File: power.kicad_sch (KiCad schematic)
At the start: 12 parts, among them SW3 SW_SPDT, U2 TP4054, U4 XC6206PxxxMR

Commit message: stm32g0
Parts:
- C6: value 0.1uF -> 100nF
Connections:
- net +5V: now also C6.2; no longer C6.1
- net GND: now also C6.1; no longer C6.2
- net at D5.1 (K), F1.2, U2.3 (V_{BAT}): now also SW3.3 (C); no longer SW3.1 (A)
- no-connect marks 2 -> 1
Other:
- moved on the sheet: BT1, C6

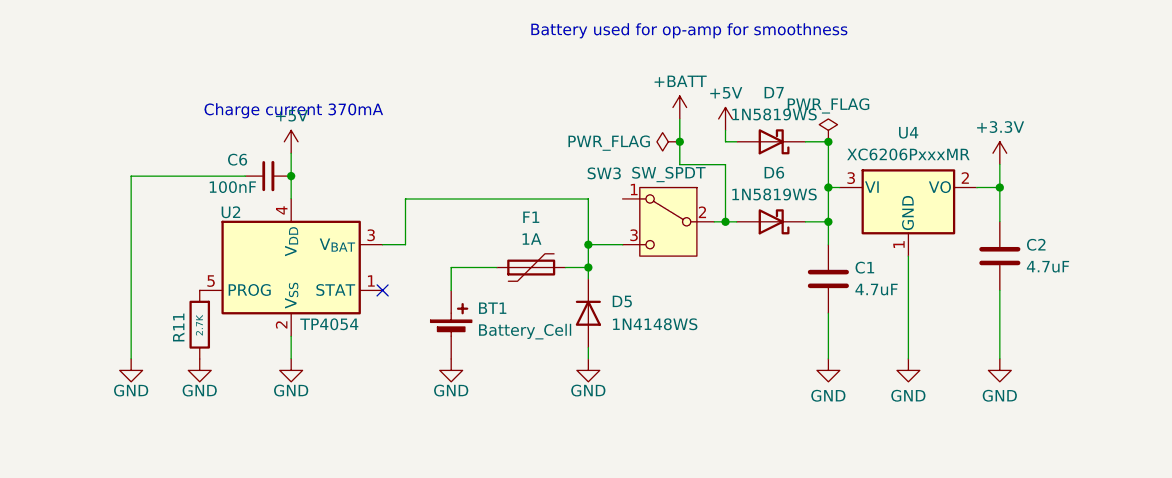
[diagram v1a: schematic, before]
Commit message: Silkscreen fixes
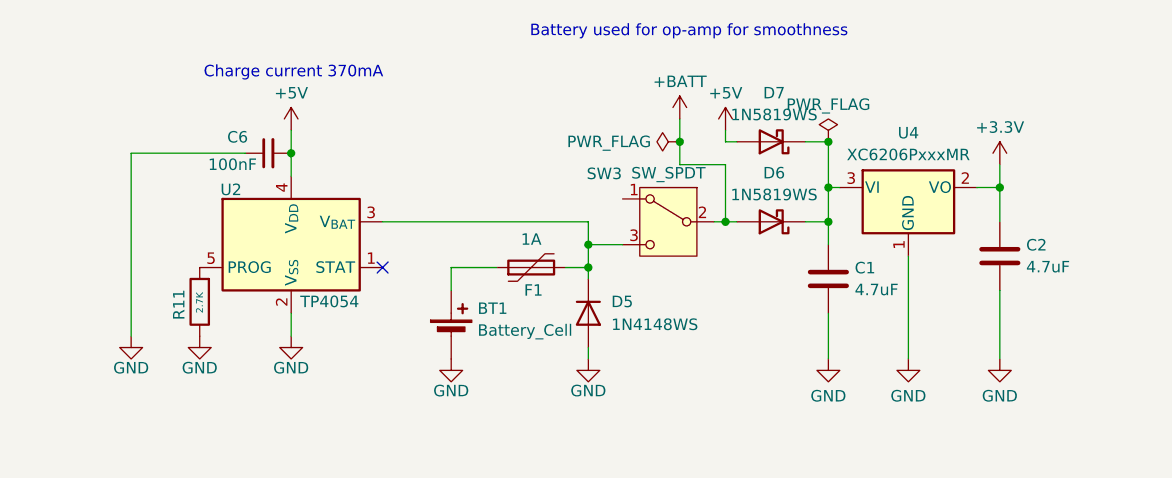
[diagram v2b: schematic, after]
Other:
- moved on the sheet: C6, R11, U2

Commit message: Added charge indicator LED, upped charge pump capacitor bank voltage rating for more headroom
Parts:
- added D1: LED, LED_SMD:LED_0805_2012Metric, symbol Device:LED
- added R1: 1K, Resistor_SMD:R_0603_1608Metric, symbol Device:R
- C1, C2: footprint Capacitor_SMD:C_0603_1608Metric_Pad1.08x0.95mm_HandSolder -> Capacitor_SMD:C_0805_2012Metric; LCSC C19666 -> C1779
- C6: value 100nF -> 1uF; LCSC C14663 -> C15849
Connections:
- net +5V: now also R1.2
- net at U2.1 (STAT): now also D1.1 (K)
- new net: D1.2 (A), R1.1
- no-connect marks 1 -> 0
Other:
- moved on the sheet: C2, R11, U2

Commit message: Fixed switch mounting holes not being grounded
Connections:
- net GND: now also SW3.4 (GND)
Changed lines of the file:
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@@
+	(wire
+		(pts
+			(xy 110.49 54.61) (xy 110.49 45.72)
+		)
+		(stroke
+			(width 0)
+			(type default)
+		)
+	)
 	(wire
 		(pts
@@
 		(in_pos_files yes)
 		(dnp no)
-		(fields_autoplaced yes)
 		(property "Reference" "D5"
-			(at 104.14 48.26 90)
+			(at 104.394 48.006 0)
 			(show_name no)
 			(do_not_autoplace no)
@@
 		)
 		(property "Value" "1N4148WS"
-			(at 104.14 50.8 90)
+			(at 106.426 48.006 0)
 			(show_name no)
 			(do_not_autoplace no)
@@
 		(pin "3"
 		)
+		(pin "4"
+		)
 		(instances
 			(project "hair-electrolysis-machine"
@@
 					(unit 1)
 				)
+			)
+		)
+	)
+	(symbol
+		(lib_id "power:GND")
+		(at 110.49 54.61 0)
+		(unit 1)
+		(body_style 1)
+		(exclude_from_sim no)
+		(in_bom yes)
+		(on_board yes)
+		(in_pos_files yes)
+		(dnp no)
+		(property "Reference" "#PWR032"
+			(at 110.49 60.96 0)
+			(hide yes)
+			(show_name no)
+			(do_not_autoplace no)
+			(effects
+				(font
+					(size 1.27 1.27)
+				)
+			)
+		)
+		(property "Value" "GND"
+			(at 110.49 58.166 0)
+			(show_name no)
+			(do_not_autoplace no)
+			(effects
+				(font
+					(size 1.27 1.27)
+				)
+			)
+		)
+		(property "Footprint" ""
+			(at 110.49 54.61 0)
+			(hide yes)
+			(show_name no)
+			(do_not_autoplace no)
+			(effects
+				(font
+					(size 1.27 1.27)
+				)
+			)
+		)
+		(property "Datasheet" ""
+			(at 110.49 54.61 0)
+			(hide yes)
+			(show_name no)
+			(do_not_autoplace no)
+			(effects
+				(font
+					(size 1.27 1.27)
+				)
+			)
+		)
+		(property "Description" "Power symbol creates a global label with name \"GND\" , ground"
+			(at 110.49 54.61 0)
+			(hide yes)
+			(show_name no)
+			(do_not_autoplace no)
+			(effects
+				(font
+					(size 1.27 1.27)
+				)
+			)
+		)
+		(pin "1"
+		)
+		(instances
+			(project "hair-electrolysis-machine"
+				(path "/724ce5ca-e5bf-4553-b755-84be7690a548/4364703c-5ced-4ab9-82a6-552a97df682c"
+					(reference "#PWR032")
+					(unit 1)
+				)

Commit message: Some minor clean ups
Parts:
- renumbered C6 to C1, C1 to C2, C2 to C3, D5 to D2, D7 to D3, D6 to D4, R11 to R1, R1 to R2, SW3 to SW1, U2 to U1, U4 to U2
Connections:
- net GND: now also SW1.MP; no longer SW1.4 (GND)
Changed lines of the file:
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@@
 		(in_pos_files yes)
 		(dnp no)
-		(property "Reference" "D5"
+		(property "Reference" "D2"
 			(at 104.394 48.006 0)
 			(show_name no)
@@
 			(project "hair-electrolysis-machine"
 				(path "/724ce5ca-e5bf-4553-b755-84be7690a548/4364703c-5ced-4ab9-82a6-552a97df682c"
-					(reference "D5")
+					(reference "D2")
 					(unit 1)
 				)
@@
 		(dnp no)
 		(fields_autoplaced yes)
-		(property "Reference" "C2"
+		(property "Reference" "C3"
 			(at 150.241 44.5078 0)
 			(show_name no)
@@
 			(project "hair-electrolysis-machine"
 				(path "/724ce5ca-e5bf-4553-b755-84be7690a548/4364703c-5ced-4ab9-82a6-552a97df682c"
-					(reference "C2")
+					(reference "C3")
 					(unit 1)
 				)
@@
 		(dnp no)
 		(fields_autoplaced yes)
-		(property "Reference" "#PWR027"
+		(property "Reference" "#PWR08"
 			(at 111.76 31.75 0)
 			(hide yes)
@@
 			(project "hair-electrolysis-machine"
 				(path "/724ce5ca-e5bf-4553-b755-84be7690a548/4364703c-5ced-4ab9-82a6-552a97df682c"
-					(reference "#PWR027")
+					(reference "#PWR08")
 					(unit 1)
 				)
@@
 		(dnp no)
 		(fields_autoplaced yes)
-		(property "Reference" "#PWR030"
+		(property "Reference" "#PWR011"
 			(at 137.16 60.96 0)
 			(hide yes)
@@
 			(project "hair-electrolysis-machine"
 				(path "/724ce5ca-e5bf-4553-b755-84be7690a548/4364703c-5ced-4ab9-82a6-552a97df682c"
-					(reference "#PWR030")
+					(reference "#PWR011")
 					(unit 1)
 				)
@@
 		(in_pos_files yes)
 		(dnp no)
-		(property "Reference" "U2"
+		(property "Reference" "U1"
 			(at 50.546 35.814 0)
 			(show_name no)
@@
 			(project "hair-electrolysis-machine"
 				(path "/724ce5ca-e5bf-4553-b755-84be7690a548/4364703c-5ced-4ab9-82a6-552a97df682c"
-					(reference "U2")
+					(reference "U1")
 					(unit 1)
 				)
@@
 		(dnp no)
 		(fields_autoplaced yes)
-		(property "Reference" "U4"
+		(property "Reference" "U2"
 			(at 137.16 29.5105 0)
 			(show_name no)
@@
 			(project "hair-electrolysis-machine"
 				(path "/724ce5ca-e5bf-4553-b755-84be7690a548/4364703c-5ced-4ab9-82a6-552a97df682c"
-					(reference "U4")
+					(reference "U2")
 					(unit 1)
 				)
@@
 		(dnp no)
 		(fields_autoplaced yes)
-		(property "Reference" "C1"
+		(property "Reference" "C2"
 			(at 131.191 44.5078 0)
 			(show_name no)
@@
 			(project "hair-electrolysis-machine"
 				(path "/724ce5ca-e5bf-4553-b755-84be7690a548/4364703c-5ced-4ab9-82a6-552a97df682c"
-					(reference "C1")
+					(reference "C2")
 					(unit 1)
 				)
@@
 		(in_pos_files yes)
 		(dnp no)
-		(property "Reference" "SW3"
+		(property "Reference" "SW1"
 			(at 103.378 34.036 0)
 			(show_name no)
@@
 		(pin "3"
 		)
-		(pin "4"
-		)
-		(instances
-			(project "hair-electrolysis-machine"
-				(path "/724ce5ca-e5bf-4553-b755-84be7690a548/4364703c-5ced-4ab9-82a6-552a97df682c"
-					(reference "SW3")
+		(pin "MP"
+		)
+		(instances
+			(project "hair-electrolysis-machine"
+				(path "/724ce5ca-e5bf-4553-b755-84be7690a548/4364703c-5ced-4ab9-82a6-552a97df682c"
+					(reference "SW1")
 					(unit 1)
 				)
@@
 		(dnp no)
 		(fields_autoplaced yes)
-		(property "Reference" "#PWR028"
+		(property "Reference" "#PWR010"
 			(at 128.27 60.96 0)
 			(hide yes)
@@
 			(project "hair-electrolysis-machine"
 				(path "/724ce5ca-e5bf-4553-b755-84be7690a548/4364703c-5ced-4ab9-82a6-552a97df682c"
-					(reference "#PWR028")
+					(reference "#PWR010")
 					(unit 1)
 				)
@@
 		(in_pos_files yes)
 		(dnp no)
-		(property "Reference" "R11"
+		(property "Reference" "R1"
 			(at 45.974 50.292 90)
 			(show_name no)
@@
 			(project "hair-electrolysis-machine"
 				(path "/724ce5ca-e5bf-4553-b755-84be7690a548/4364703c-5ced-4ab9-82a6-552a97df682c"
-					(reference "R11")
+					(reference "R1")
 					(unit 1)
 				)
@@
 		(dnp no)
 		(fields_autoplaced yes)
-		(property "Reference" "#PWR031"
+		(property "Reference" "#PWR012"
 			(at 147.32 36.83 0)
 			(hide yes)
@@
 			(project "hair-electrolysis-machine"
 				(path "/724ce5ca-e5bf-4553-b755-84be7690a548/4364703c-5ced-4ab9-82a6-552a97df682c"
-					(reference "#PWR031")
+					(reference "#PWR012")
 					(unit 1)
 				)
@@
 		(dnp no)
 		(fields_autoplaced yes)
-		(property "Reference" "D7"
+		(property "Reference" "D3"
 			(at 122.2375 25.0655 0)
 			(show_name no)
@@
 			(project "hair-electrolysis-machine"
 				(path "/724ce5ca-e5bf-4553-b755-84be7690a548/4364703c-5ced-4ab9-82a6-552a97df682c"
-					(reference "D7")
+					(reference "D3")
 					(unit 1)
 				)
@@
 		(in_pos_files yes)
 		(dnp no)
-		(property "Reference" "#PWR04"
+		(property "Reference" "#PWR01"
 			(at 40.64 58.42 0)
 			(hide yes)
@@
 			(project "hair-electrolysis-machine"
 				(path "/724ce5ca-e5bf-4553-b755-84be7690a548/4364703c-5ced-4ab9-82a6-552a97df682c"
-					(reference "#PWR04")
+					(reference "#PWR01")
 					(unit 1)
 				)
@@
 		(in_pos_files yes)
 		(dnp no)
-		(property "Reference" "#PWR032"
+		(property "Reference" "#PWR07"
 			(at 110.49 60.96 0)
 			(hide yes)
@@
 			(project "hair-electrolysis-machine"
 				(path "/724ce5ca-e5bf-4553-b755-84be7690a548/4364703c-5ced-4ab9-82a6-552a97df682c"
-					(reference "#PWR032")
+					(reference "#PWR07")
 					(unit 1)
 				)
@@
 		(in_pos_files yes)
 		(dnp no)
-		(property "Reference" "R1"
+		(property "Reference" "R2"
 			(at 67.31 29.464 90)
 			(show_name no)
@@
 			(project "hair-electrolysis-machine"
 				(path "/724ce5ca-e5bf-4553-b755-84be7690a548/4364703c-5ced-4ab9-82a6-552a97df682c"
-					(reference "R1")
+					(reference "R2")
 					(unit 1)
 				)
@@
 		(in_pos_files yes)
 		(dnp no)
-		(property "Reference" "C6"
+		(property "Reference" "C1"
 			(at 52.07 33.274 90)
 			(show_name no)
@@
 			(project "hair-electrolysis-machine"
 				(path "/724ce5ca-e5bf-4553-b755-84be7690a548/4364703c-5ced-4ab9-82a6-552a97df682c"
-					(reference "C6")
+					(reference "C1")
 					(unit 1)
 				)
@@
 		(dnp no)
 		(fields_autoplaced yes)
-		(property "Reference" "#PWR01"
+		(property "Reference" "#PWR03"
 			(at 58.42 33.02 0)
 			(hide yes)
@@
 			(project "hair-electrolysis-machine"
 				(path "/724ce5ca-e5bf-4553-b755-84be7690a548/4364703c-5ced-4ab9-82a6-552a97df682c"
-					(reference "#PWR01")
+					(reference "#PWR03")
 					(unit 1)
 				)
@@
 		(dnp no)
 		(fields_autoplaced yes)
-		(property "Reference" "#PWR03"
+		(property "Reference" "#PWR09"
 			(at 116.84 33.02 0)
 			(hide yes)
@@
 			(project "hair-electrolysis-machine"
 				(path "/724ce5ca-e5bf-4553-b755-84be7690a548/4364703c-5ced-4ab9-82a6-552a97df682c"
-					(reference "#PWR03")
+					(reference "#PWR09")
 					(unit 1)
 				)
@@
 		(in_pos_files yes)
 		(dnp no)
-		(property "Reference" "D6"
+		(property "Reference" "D4"
 			(at 122.2375 33.9555 0)
 			(show_name no)
@@
 			(project "hair-electrolysis-machine"
 				(path "/724ce5ca-e5bf-4553-b755-84be7690a548/4364703c-5ced-4ab9-82a6-552a97df682c"
-					(reference "D6")
+					(reference "D4")
 					(unit 1)
 				)
@@
 		(in_pos_files yes)
 		(dnp no)
-		(property "Reference" "#PWR044"
+		(property "Reference" "#PWR06"
 			(at 101.6 60.96 0)
 			(hide yes)
@@
 			(project "hair-electrolysis-machine"
 				(path "/724ce5ca-e5bf-4553-b755-84be7690a548/4364703c-5ced-4ab9-82a6-552a97df682c"
-					(reference "#PWR044")
+					(reference "#PWR06")
 					(unit 1)
 				)
@@
 		(in_pos_files yes)
 		(dnp no)
-		(property "Reference" "#PWR024"
+		(property "Reference" "#PWR04"
 			(at 58.42 58.42 0)
 			(hide yes)
@@
 			(project "hair-electrolysis-machine"
 				(path "/724ce5ca-e5bf-4553-b755-84be7690a548/4364703c-5ced-4ab9-82a6-552a97df682c"
-					(reference "#PWR024")
+					(reference "#PWR04")
 					(unit 1)
 				)
@@
 		(in_pos_files yes)
 		(dnp no)
-		(property "Reference" "#PWR026"
+		(property "Reference" "#PWR05"
 			(at 86.36 60.96 0)
 			(hide yes)
@@
 			(project "hair-electrolysis-machine"
 				(path "/724ce5ca-e5bf-4553-b755-84be7690a548/4364703c-5ced-4ab9-82a6-552a97df682c"
-					(reference "#PWR026")
+					(reference "#PWR05")
 					(unit 1)
 				)
@@
 		(dnp no)
 		(fields_autoplaced yes)
-		(property "Reference" "#PWR029"
+		(property "Reference" "#PWR013"
 			(at 147.32 60.96 0)
 			(hide yes)
@@
 			(project "hair-electrolysis-machine"
 				(path "/724ce5ca-e5bf-4553-b755-84be7690a548/4364703c-5ced-4ab9-82a6-552a97df682c"
-					(reference "#PWR029")
-					(unit 1)
-				)
+					(reference "#PWR013")
+					(unit 1)
+				)

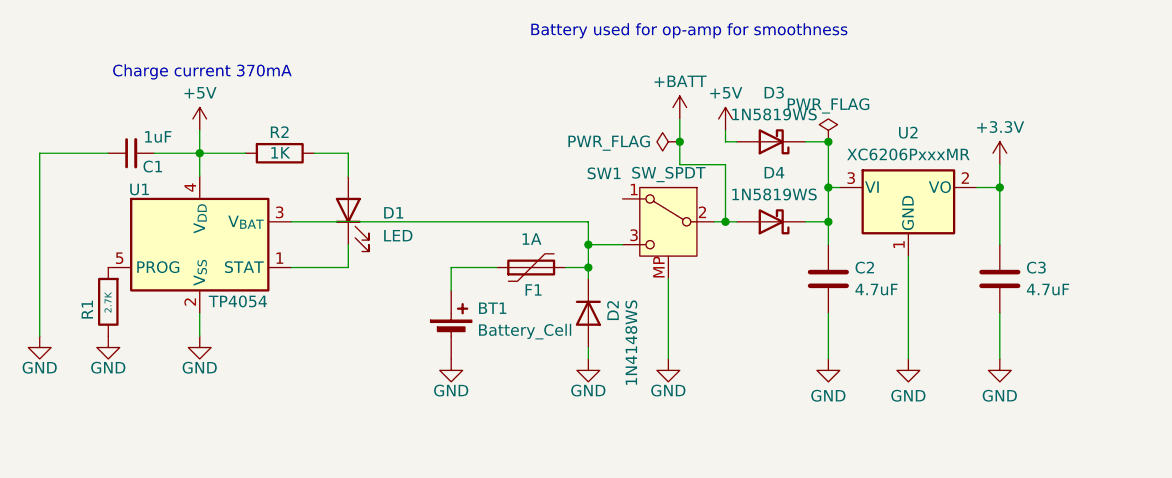
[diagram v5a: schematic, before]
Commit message: change jack pinout and charge limiting
limit charge speed to be more conservative and change jack pins used so there's zero overlap between pedal and stylus
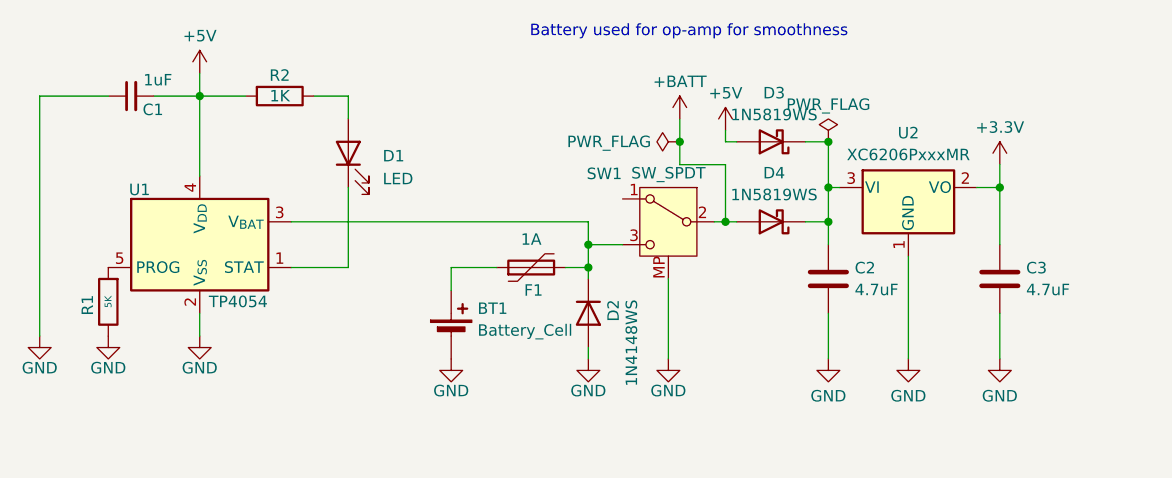
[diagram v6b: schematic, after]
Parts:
- R1: value 2.7K -> 5K; LCSC C13167 -> C862232
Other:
- note removed: "Charge current 370mA"
- moved on the sheet: C1, D1, R2
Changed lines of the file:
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@@
 	(generator_version "10.0")
 	(paper "A4")
-	(text "Charge current 370mA"
-		(exclude_from_sim no)
-		(at 58.674 22.86 0)
-		(effects
-			(font
-				(size 1.27 1.27)
-			)
-		)
-	)
 	(text "Battery used for op-amp for smoothness"
 		(exclude_from_sim no)
@@
 	)
 	(junction
-		(at 58.42 31.75)
+		(at 58.42 25.4)
 		(diameter 0)
 		(color 0 0 0 0)
@@
 	(wire
 		(pts
-			(xy 74.93 41.91) (xy 74.93 44.45)
+			(xy 74.93 25.4) (xy 74.93 27.94)
+		)
+		(stroke
+			(width 0)
+			(type default)
+		)
+	)
+	(wire
+		(pts
+			(xy 74.93 35.56) (xy 74.93 44.45)
 		)
 		(stroke
@@
 	(wire
 		(pts
-			(xy 74.93 31.75) (xy 71.12 31.75)
+			(xy 74.93 25.4) (xy 71.12 25.4)
 		)
 		(stroke
@@
 	(wire
 		(pts
-			(xy 53.34 31.75) (xy 58.42 31.75)
+			(xy 58.42 25.4) (xy 58.42 34.29)
+		)
+		(stroke
+			(width 0)
+			(type default)
+		)
+	)
+	(wire
+		(pts
+			(xy 53.34 25.4) (xy 58.42 25.4)
 		)
 		(stroke
@@
 	(wire
 		(pts
-			(xy 48.26 31.75) (xy 40.64 31.75)
+			(xy 48.26 25.4) (xy 40.64 25.4)
 		)
 		(stroke
@@
 	(wire
 		(pts
-			(xy 40.64 31.75) (xy 40.64 52.07)
+			(xy 40.64 25.4) (xy 40.64 52.07)
 		)
 		(stroke
@@
 	(wire
 		(pts
-			(xy 58.42 29.21) (xy 58.42 31.75)
+			(xy 58.42 22.86) (xy 58.42 25.4)
 		)
 		(stroke
@@
 	(wire
 		(pts
-			(xy 63.5 31.75) (xy 58.42 31.75)
+			(xy 63.5 25.4) (xy 58.42 25.4)
 		)
 		(stroke
@@
 	(wire
 		(pts
-			(xy 58.42 31.75) (xy 58.42 34.29)
-		)
-		(stroke
-			(width 0)
-			(type default)
-		)
-	)
-	(wire
-		(pts
 			(xy 128.27 39.37) (xy 128.27 41.91)
 		)
@@
 		(pts
 			(xy 125.73 30.48) (xy 128.27 30.48)
-		)
-		(stroke
-			(width 0)
-			(type default)
-		)
-	)
-	(wire
-		(pts
-			(xy 74.93 34.29) (xy 74.93 31.75)
 		)
 		(stroke
@@
 	(symbol
 		(lib_id "Device:LED")
-		(at 74.93 38.1 90)
+		(at 74.93 31.75 90)
 		(unit 1)
 		(body_style 1)
@@
 		(fields_autoplaced yes)
 		(property "Reference" "D1"
-			(at 78.74 38.4174 90)
+			(at 78.74 32.0674 90)
 			(show_name no)
 			(do_not_autoplace no)
@@
 		)
 		(property "Value" "LED"
-			(at 78.74 40.9574 90)
+			(at 78.74 34.6074 90)
 			(show_name no)
 			(do_not_autoplace no)
@@
 		)
 		(property "Footprint" "LED_SMD:LED_0805_2012Metric"
-			(at 74.93 38.1 0)
+			(at 74.93 31.75 0)
 			(hide yes)
 			(show_name no)
@@
 		)
 		(property "Datasheet" ""
-			(at 74.93 38.1 0)
+			(at 74.93 31.75 0)
 			(hide yes)
 			(show_name no)
@@
 		)
 		(property "Description" "Light emitting diode"
-			(at 74.93 38.1 0)
+			(at 74.93 31.75 0)
 			(hide yes)
 			(show_name no)
@@
 		)
 		(property "Sim.Pins" "1=K 2=A"
-			(at 74.93 38.1 0)
+			(at 74.93 31.75 0)
 			(hide yes)
 			(show_name no)
@@
 		)
 		(property "LCSC" "C84256"
-			(at 74.93 38.1 90)
+			(at 74.93 31.75 90)
 			(hide yes)
 			(show_name no)
@@
 		(dnp no)
 		(property "Reference" "R1"
-			(at 45.974 50.292 90)
+			(at 45.974 49.784 90)
 			(show_name no)
 			(do_not_autoplace no)
@@
 			)
 		)
-		(property "Value" "2.7K"
-			(at 48.26 49.53 90)
+		(property "Value" "5K"
+			(at 48.26 48.26 90)
 			(show_name no)
 			(do_not_autoplace no)
@@
 					(size 0.762 0.762)
 				)
-				(justify right)
 			)
 		)
@@
 			)
 		)
-		(property "LCSC" "C13167"
+		(property "LCSC" "C862232"
 			(at 48.26 48.26 0)
 			(hide yes)
@@
 	(symbol
 		(lib_id "Device:R")
-		(at 67.31 31.75 270)
+		(at 67.31 25.4 270)
 		(unit 1)
 		(body_style 1)
@@
 		(dnp no)
 		(property "Reference" "R2"
-			(at 67.31 29.464 90)
+			(at 67.31 23.114 90)
 			(show_name no)
 			(do_not_autoplace no)
@@
 		)
 		(property "Value" "1K"
-			(at 67.31 31.75 90)
+			(at 67.31 25.4 90)
 			(show_name no)
 			(do_not_autoplace no)
@@
 		)
 		(property "Footprint" "Resistor_SMD:R_0603_1608Metric"
-			(at 67.31 29.972 90)
+			(at 67.31 23.622 90)
 			(hide yes)
 			(show_name no)
@@
 		)
 		(property "Datasheet" ""
-			(at 67.31 31.75 0)
+			(at 67.31 25.4 0)
 			(hide yes)
 			(show_name no)
@@
 		)
 		(property "Description" "Resistor"
-			(at 67.31 31.75 0)
+			(at 67.31 25.4 0)
 			(hide yes)
 			(show_name no)
@@
 		)
 		(property "LCSC" "C21190"
-			(at 67.31 31.75 90)
+			(at 67.31 25.4 90)
 			(hide yes)
 			(show_name no)
@@
 	(symbol
 		(lib_id "Device:C_Small")
-		(at 50.8 31.75 90)
+		(at 50.8 25.4 90)
 		(unit 1)
 		(body_style 1)
@@
 		(dnp no)
 		(property "Reference" "C1"
-			(at 52.07 33.274 90)
+			(at 52.07 26.924 90)
 			(show_name no)
 			(do_not_autoplace no)
@@
 		)
 		(property "Value" "1uF"
-			(at 55.372 29.972 90)
+			(at 55.372 23.622 90)
 			(show_name no)
 			(do_not_autoplace no)
@@
 		)
 		(property "Footprint" "Capacitor_SMD:C_0603_1608Metric"
-			(at 50.8 31.75 0)
+			(at 50.8 25.4 0)
 			(hide yes)
 			(show_name no)
@@
 		)
 		(property "Datasheet" ""
-			(at 50.8 31.75 0)
+			(at 50.8 25.4 0)
 			(hide yes)
 			(show_name no)
@@
 		)
 		(property "Description" "Unpolarized capacitor, small symbol"
-			(at 50.8 31.75 0)
+			(at 50.8 25.4 0)
 			(hide yes)
 			(show_name no)
@@
 		)
 		(property "LCSC" "C15849"
-			(at 50.8 31.75 90)
+			(at 50.8 25.4 90)
 			(hide yes)
 			(show_name no)
@@
 	(symbol
 		(lib_id "power:+5V")
-		(at 58.42 29.21 0)
+		(at 58.42 22.86 0)
 		(unit 1)
 		(body_style 1)
@@
 		(fields_autoplaced yes)
 		(property "Reference" "#PWR03"
-			(at 58.42 33.02 0)
+			(at 58.42 26.67 0)
 			(hide yes)
 			(show_name no)
@@
 		)
 		(property "Value" "+5V"
-			(at 58.42 25.0769 0)
+			(at 58.42 18.7269 0)
 			(show_name no)
 			(do_not_autoplace no)
@@
 		)
 		(property "Footprint" ""
-			(at 58.42 29.21 0)
+			(at 58.42 22.86 0)
 			(hide yes)
 			(show_name no)
@@
 		)
 		(property "Datasheet" ""
-			(at 58.42 29.21 0)
+			(at 58.42 22.86 0)
 			(hide yes)
 			(show_name no)
@@
 		)
 		(property "Description" "Power symbol creates a global label with name \"+5V\""
-			(at 58.42 29.21 0)
-			(hide yes)
-			(show_name no)
+			(at 58.42 22.86 0)
+			(hide yes)
+			(show_name no)
